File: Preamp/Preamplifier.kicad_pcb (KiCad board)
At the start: 2 copper layers, 100 x 100 mm, 155 parts, among them J1 Conn_01x03_Male, J12 XLR3, J14 Conn_01x03, J15 Conn_01x02, J16 Conn_01x02, J17 Conn_01x02, J2 Conn_01x02_Male, J3 Conn_01x02_Male, J4 Conn_01x03_Male, J5 Conn_01x03_Male, J6 Conn_01x02_Male, J7 Conn_01x03, J8 Conn_01x05_Female, Q1 2N3904, Q2 2N3906, Q3 2N3904, Q4 2N3906, Q5 BC549, SW1 SW_DPST, SW2 SW_SPDT, SW3 GND LIFT, SW4 SW_SPST, SW5 SW_HPFQ, U1 OPA2134, U2 NE5532, U3 NE5532, U4 NE5532, U5 TL072, U6 NE5532, U7 NE5532, U8 NE5532, U9 NE5532

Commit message: More layout work
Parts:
- removed C17: 100uF 50V, Capacitor_THT:CP_Radial_D8.0mm_P3.50mm
- removed C20, C21: 0.1uF, Capacitor_SMD:C_0805_2012Metric_Pad1.15x1.40mm_HandSolder
- removed D3, D4: 1N4148, Diode_THT:D_DO-35_SOD27_P7.62mm_Horizontal
- removed Q1: 2N3904, Package_TO_SOT_THT:TO-92_Inline
- removed Q2: 2N3906, Package_TO_SOT_THT:TO-92_Inline
- removed R15: 22k, Resistor_SMD:R_0805_2012Metric_Pad1.15x1.40mm_HandSolder
- removed R18, R23: 10K, Resistor_SMD:R_0805_2012Metric_Pad1.15x1.40mm_HandSolder
- removed R25, R26: 3.9k, Resistor_SMD:R_0805_2012Metric_Pad1.15x1.40mm_HandSolder
- removed R31: 10k, Resistor_SMD:R_0805_2012Metric_Pad1.15x1.40mm_HandSolder
- removed U3: NE5532, Package_DIP:DIP-8_W7.62mm_Socket
- C12, C15, C24, R10, R12, R20, R21, R42, R9: moved to B.Cu
- R11: value 10k -> 12k
- RV1: footprint Connector_PinHeader_2.54mm:PinHeader_2x03_P2.54mm_Vertical -> Connector_PinHeader_2.54mm:PinHeader_1x06_P2.54mm_Vertical
- RV2: value 1K log (headphone vol) -> 10k log (headphone vol); footprint Connector_PinHeader_2.54mm:PinHeader_2x03_P2.54mm_Vertical -> Connector_PinHeader_2.54mm:PinHeader_1x03_P2.54mm_Vertical
- SW1: value SW_DPST -> SW_HPF
- moved SW5 337.8 mm to (45.7, 94.9), turned to 270 degrees
- moved SW1 335.2 mm to (38.1, 94.9), turned to 270 degrees
- moved C1 281.9 mm to (130.8, 76.4), turned to 270 degrees
- moved C2 281.3 mm to (122.7, 76.4), turned to 270 degrees
- moved R9 268.9 mm to (128.3, 77.3), turned to 90 degrees
- moved C3 155.9 mm to (27.7, 86.1)
- moved R12 151.3 mm to (40.6, 96.5), turned to 90 degrees
- moved C6 148.7 mm to (31.9, 91.1)
- moved R13 145.2 mm to (32.0, 83.6), turned to 180 degrees
- moved C16 134.3 mm to (38.0, 89.3), turned to 90 degrees
- moved U2 131.0 mm to (35.7, 82.9), turned to 0 degrees
- moved C15 123.0 mm to (40.8, 83.9), turned to 90 degrees
- moved C9 121.6 mm to (46.6, 90.1), turned to 0 degrees
- moved R65 119.4 mm to (49.0, 91.1), turned to 270 degrees
- moved R17 115.1 mm to (49.0, 87.9), turned to 0 degrees
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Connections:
- R11 pad 1: EFXreturn -> GNDD
- R11 pad 2: Net-(R10-Pad2) -> GND
- R33 pad 1: Net-(R33-Pad1) -> Net-(J5-Pad3)
- R33 pad 2: Net-(C17-Pad2) -> Net-(R33-Pad2)
- R34 pad 1: Net-(R34-Pad1) -> Net-(J5-Pad2)
- R34 pad 2: Net-(C14-Pad2) -> Net-(R33-Pad2)
- R8 pad 2: Net-(R15-Pad1) -> Net-(R10-Pad2)
- R9 pad 2: Net-(R15-Pad1) -> Net-(R10-Pad2)
- RV2 pad 1: Net-(R33-Pad1) -> Net-(C14-Pad2)
- RV2 pad 2: Net-(J5-Pad3) -> Net-(R33-Pad2)
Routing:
- net Net-(C33-Pad2): track 37.5 -> 0.00 mm
- net -12V: track 132.5 -> 102.0 mm, vias 4 -> 1
- net Net-(C7-Pad2): track 17.4 -> 41.6 mm, vias 0 -> 1
- net Net-(C3-Pad1): track 0.00 -> 22.3 mm, vias 0 -> 1
- net Net-(C6-Pad1): track 0.00 -> 18.7 mm, vias 0 -> 1
- net +12V: track 129.5 -> 112.5 mm, vias 2 -> 3
- net FromEQ: track 0.00 -> 15.7 mm, vias 0 -> 1
- net LF: track 45.1 -> 30.3 mm
- net GND: track 7.90 -> 22.5 mm
- net GNDD: track 8.48 -> 19.0 mm
- net Net-(C7-Pad1): track 5.77 -> 15.0 mm
- net HF: track 18.6 -> 9.42 mm
- net Net-(C9-Pad1): track 5.89 -> 14.6 mm
- net Net-(C1-Pad2): track 0.00 -> 7.00 mm
- net Net-(C42-Pad2): track 6.00 -> 0.00 mm
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
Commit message: More layout
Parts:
- added H1: MountingHole, MountingHole:MountingHole_3.2mm_M3_ISO7380, F.Cu at (4.00, 96.0)
- added H2: MountingHole, MountingHole:MountingHole_3.2mm_M3_ISO7380, F.Cu at (103.3, 1.08)
- added H3: MountingHole, MountingHole:MountingHole_3.2mm_M3_ISO7380, F.Cu at (110.5, -6.17)
- added H4: MountingHole, MountingHole:MountingHole_3.2mm_M3_ISO7380, F.Cu at (110.5, 1.08)
- added J9: Conn_01x03, Connector_PinHeader_2.54mm:PinHeader_1x03_P2.54mm_Vertical, F.Cu at (5.08, 59.4)
- C36, C37, R29, R37, R38, R41, R44, R63: moved to B.Cu
- moved R37 365.7 mm to (35.6, 52.6), turned to 270 degrees
- moved D11 282.7 mm to (48.5, 115.7)
- moved SW3 121.4 mm to (58.4, 51.7), turned to 0 degrees
- moved J12 120.7 mm to (48.3, 51.7)
- moved R38 113.1 mm to (30.6, 52.2), turned to 270 degrees
- moved R41 108.5 mm to (26.6, 62.7), turned to 180 degrees
- moved R40 107.1 mm to (23.0, 55.6), turned to 270 degrees
- moved U6 106.6 mm to (27.8, 60.5), turned to 270 degrees
- moved C41 105.3 mm to (42.7, 73.8)
- moved C42 105.3 mm to (33.7, 73.8)
- moved C43 105.3 mm to (42.7, 61.2)
- moved C44 105.3 mm to (33.7, 61.2)
- moved C36 101.1 mm to (28.8, 66.1)
- moved R45 100.6 mm to (24.8, 71.1), turned to 180 degrees
- moved C37 100.4 mm to (20.1, 63.4), turned to 270 degrees
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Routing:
- net PreEQ: track 30.5 -> 66.7 mm, vias 1 -> 2
- net -12V: track 102.0 -> 132.5 mm
- net EFXreturn: track 16.0 -> 43.0 mm, vias 1 -> 3
- net Net-(D16-Pad2): track 9.51 -> 31.4 mm, vias 0 -> 1
- net LF: track 30.3 -> 8.67 mm, vias 1 -> 0
- net Net-(C44-Pad1): track 2.78 -> 23.6 mm
- net +12V: track 112.5 -> 133.2 mm
- net Tweeter: track 4.67 -> 19.0 mm
- net Net-(R38-Pad2): track 2.81 -> 16.5 mm
- net Net-(C43-Pad1): track 6.71 -> 17.0 mm
- net Net-(D11-Pad2): track 18.4 -> 28.2 mm, vias 0 -> 2
- net GND: track 22.5 -> 32.1 mm, vias 11 -> 9
- net Net-(C33-Pad2): track 0.00 -> 7.94 mm
- net GNDD: track 19.0 -> 11.4 mm
- net Net-(RV3-Pad1): track 0.00 -> 6.13 mm
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
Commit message: More layout work
Still need to lay out the headphone amplifier.
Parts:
- removed J7: Conn_01x03, TerminalBlock_Phoenix:TerminalBlock_Phoenix_MKDS-1,5-3_1x03_P5.00mm_Horizontal
- C22, R11, R30, R35, R36, R39, R43, R61, R64: moved to B.Cu
- D2: footprint Diode_THT:D_DO-35_SOD27_P7.62mm_Horizontal -> Diode_SMD:D_SOD-123; moved to B.Cu
- R48: moved to F.Cu
- moved R61 377.3 mm to (33.2, 96.6), turned to 270 degrees
- moved R30 369.8 mm to (39.5, 63.1), turned to 270 degrees
- moved R64 366.3 mm to (41.1, 89.2), turned to 270 degrees
- moved R39 361.0 mm to (56.6, 82.7), turned to 180 degrees
- moved R36 360.2 mm to (58.3, 87.0), turned to 180 degrees
- moved C22 355.6 mm to (66.3, 89.4), turned to 270 degrees
- moved C11 330.4 mm to (50.5, 80.0), turned to 90 degrees
- moved R35 328.3 mm to (62.4, 87.0), turned to 180 degrees
- moved R43 322.8 mm to (61.6, 98.8), turned to 180 degrees
- moved Q4 209.0 mm to (213.8, 74.4)
- moved C14 209.0 mm to (156.5, 96.6)
- moved Q3 209.0 mm to (188.8, 98.8)
- moved R27 209.0 mm to (197.3, 105.2)
- moved R28 209.0 mm to (185.4, 116.8)
- moved R32 209.0 mm to (209.3, 92.3)
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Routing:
- net +12V: track 133.2 -> 205.4 mm
- net -12V: track 132.5 -> 177.3 mm, vias 1 -> 3
- net LF: track 8.67 -> 52.7 mm
- net Net-(C5-Pad2): track 9.07 -> 43.7 mm, vias 0 -> 2
- net Overload: track 0.00 -> 33.1 mm
- net GNDD: track 11.4 -> 38.1 mm, vias 0 -> 2
- net Net-(C11-Pad2): track 0.00 -> 19.3 mm
- net Net-(D11-Pad2): track 28.2 -> 47.0 mm
- net Net-(R64-Pad2): track 0.00 -> 13.7 mm, vias 0 -> 3
- net HF: track 9.42 -> 23.1 mm
- net Net-(C11-Pad1): track 7.23 -> 19.4 mm
- net EFXsend: track 5.08 -> 13.0 mm, vias 0 -> 1
- net Net-(R35-Pad2): track 0.00 -> 4.60 mm
- net GND: track 32.1 -> 36.3 mm, vias 9 -> 11
- net Net-(C22-Pad2): track 4.80 -> 8.21 mm
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
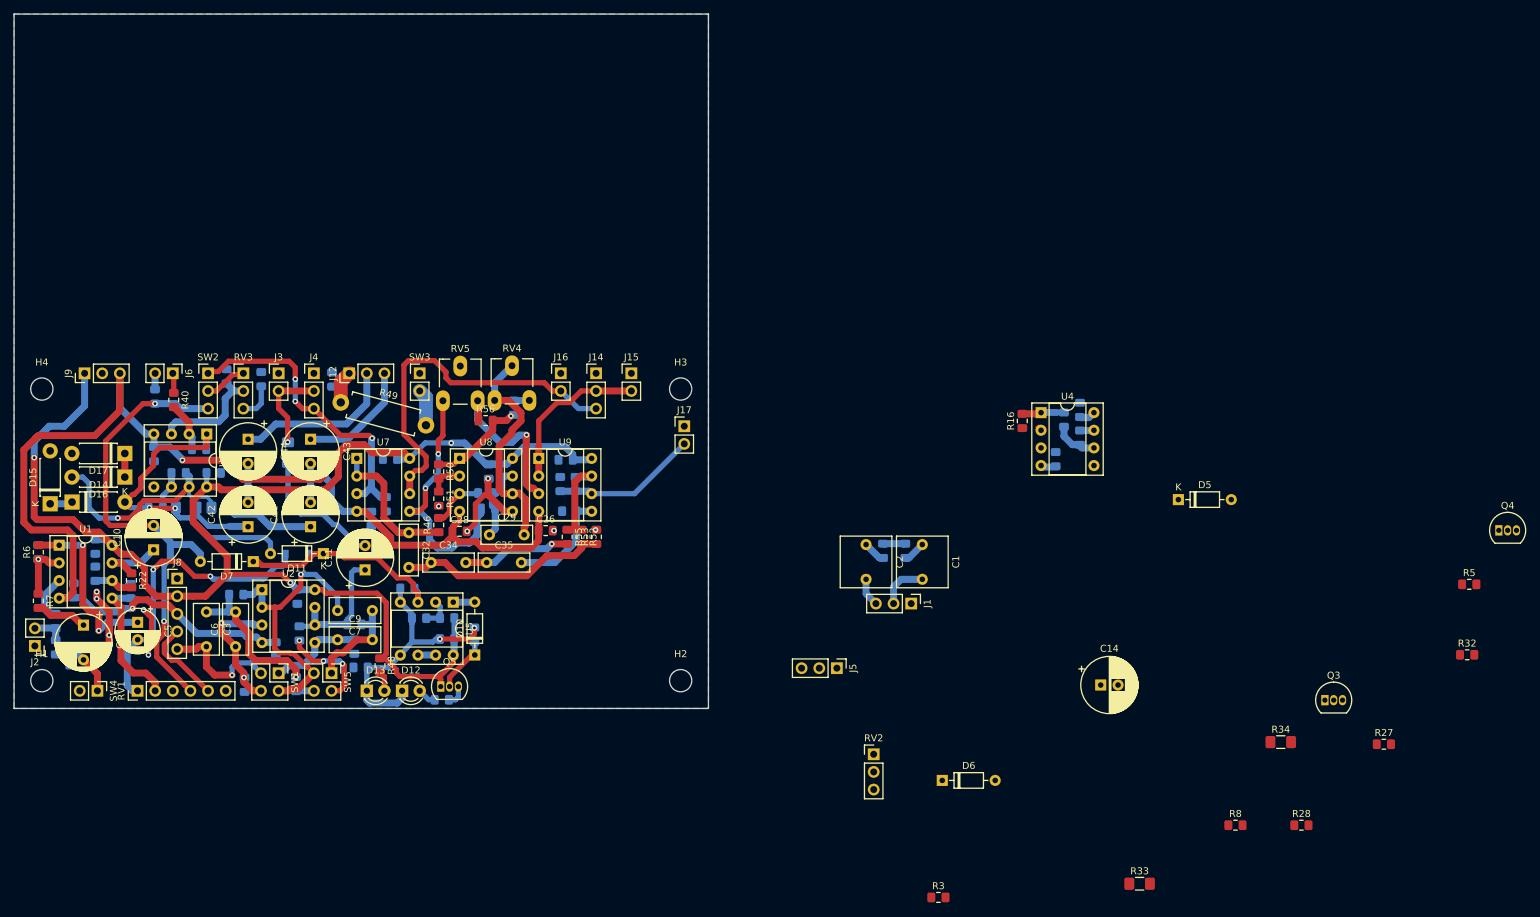
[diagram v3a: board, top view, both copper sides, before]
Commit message: Finished first pass at layout.
Still need to clean up silkscreen.
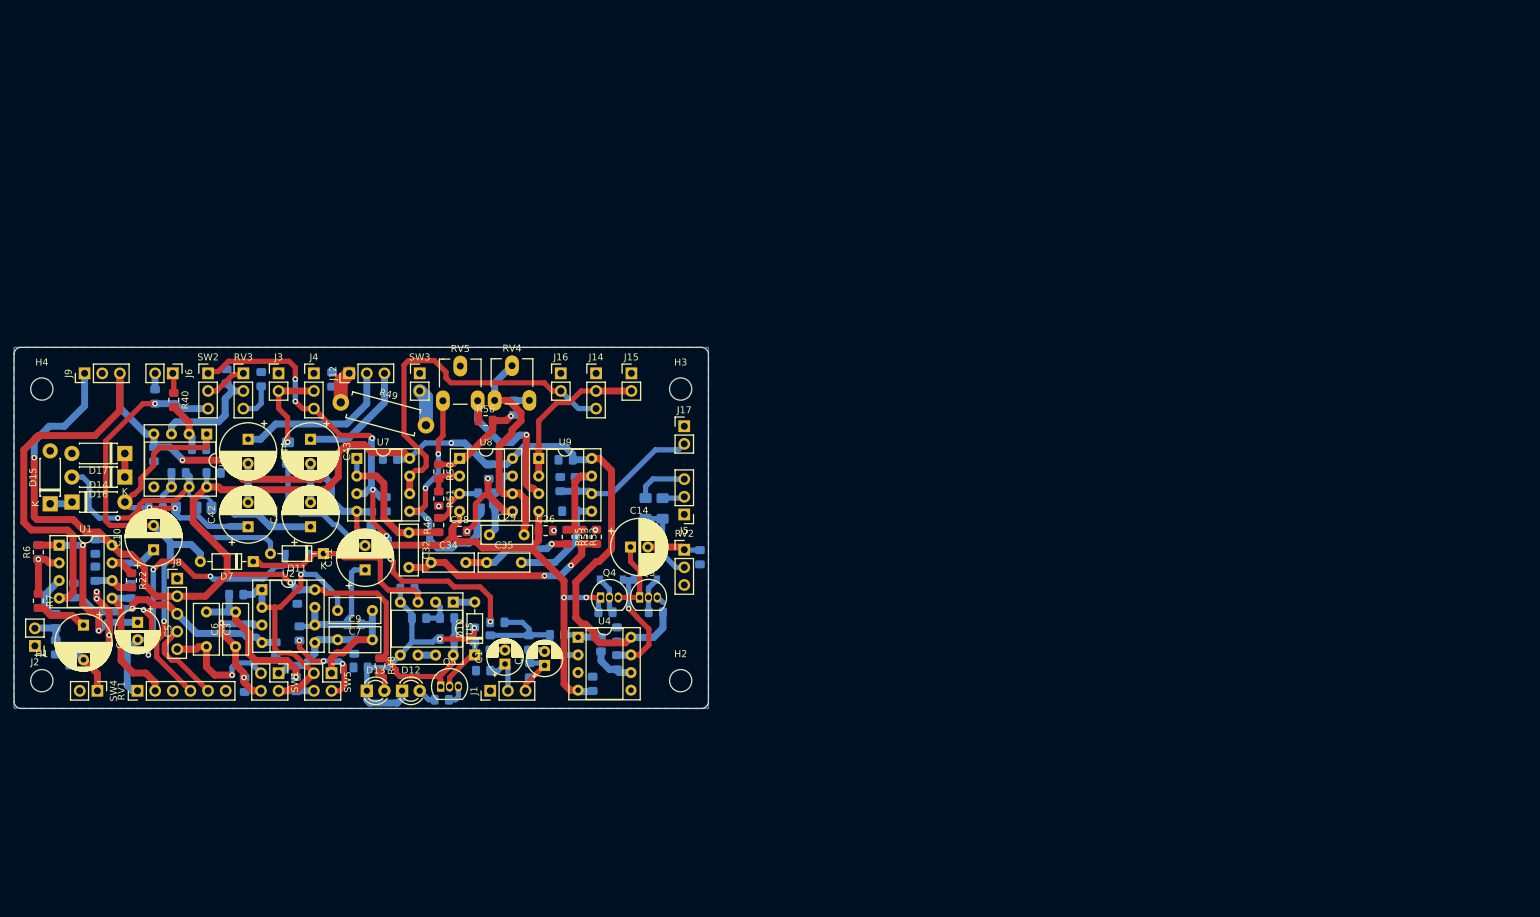
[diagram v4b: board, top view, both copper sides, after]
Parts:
- C1, C2: value 1uF -> 10uF 35V; footprint Capacitor_THT:C_Rect_L7.2mm_W7.2mm_P5.00mm_FKS2_FKP2_MKS2_MKP2 -> Capacitor_THT:CP_Radial_D5.0mm_P2.00mm
- D5, D6: footprint Diode_THT:D_DO-35_SOD27_P7.62mm_Horizontal -> Diode_SMD:D_SOD-123; moved to B.Cu
- R16, R27, R28, R3, R32, R33, R34, R5, R8: moved to B.Cu
- moved R5 142.6 mm to (67.5, 94.5), turned to 180 degrees
- moved Q4 129.7 mm to (84.5, 84.0)
- moved R32 111.4 mm to (98.8, 78.2), turned to 270 degrees
- moved R8 110.2 mm to (69.6, 87.6)
- moved R27 106.6 mm to (92.4, 86.2), turned to 180 degrees
- moved R28 104.8 mm to (85.2, 86.2), turned to 180 degrees
- moved Q3 99.8 mm to (90.1, 84.0)
- moved R34 95.2 mm to (93.4, 71.2), turned to 270 degrees
- moved R33 89.4 mm to (91.0, 71.2), turned to 270 degrees
- moved D5 77.6 mm to (90.9, 81.5)
- moved C19 74.1 mm to (83.3, 96.5)
- moved U4 74.1 mm to (81.2, 89.8)
- moved C18 74.1 mm to (86.8, 89.3)
- moved R19 74.1 mm to (84.5, 90.8)
- moved R24 74.1 mm to (86.8, 93.3)
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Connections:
- J1 pad 2: Net-(C1-Pad2) -> Net-(C1-Pad1)
- J1 pad 3: Net-(C2-Pad2) -> Net-(C2-Pad1)
- R10 pad 1: Net-(C2-Pad1) -> Net-(C2-Pad2)
- R3 pad 1: Net-(C2-Pad2) -> Net-(C2-Pad1)
- R5 pad 1: Net-(C1-Pad2) -> Net-(C1-Pad1)
- R9 pad 1: Net-(C1-Pad1) -> Net-(C1-Pad2)
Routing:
- net +12V: track 205.4 -> 251.3 mm
- net -12V: track 177.3 -> 210.4 mm, vias 3 -> 5
- net EFXreturn: track 44.1 -> 76.3 mm, vias 3 -> 7
- net Net-(R10-Pad2): track 3.65 -> 19.4 mm
- net Net-(D5-Pad1): track 2.03 -> 17.4 mm, vias 0 -> 1
- net Net-(R33-Pad2): track 0.00 -> 11.4 mm
- net Net-(C14-Pad1): track 0.00 -> 10.9 mm
- net Net-(J5-Pad3): track 0.00 -> 7.72 mm
- net Net-(C14-Pad2): track 0.00 -> 7.69 mm
- net Net-(D6-Pad1): track 0.00 -> 5.46 mm
- net Net-(D5-Pad2): track 0.00 -> 5.22 mm
- net Net-(C1-Pad2): track 7.00 -> 2.13 mm
- net Net-(C2-Pad1): track 3.25 -> 7.08 mm
- net Net-(C1-Pad1): track 3.25 -> 6.55 mm
- net Net-(J5-Pad2): track 0.00 -> 3.20 mm
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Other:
- board size 100 x 100 mm -> 100 x 52 mm

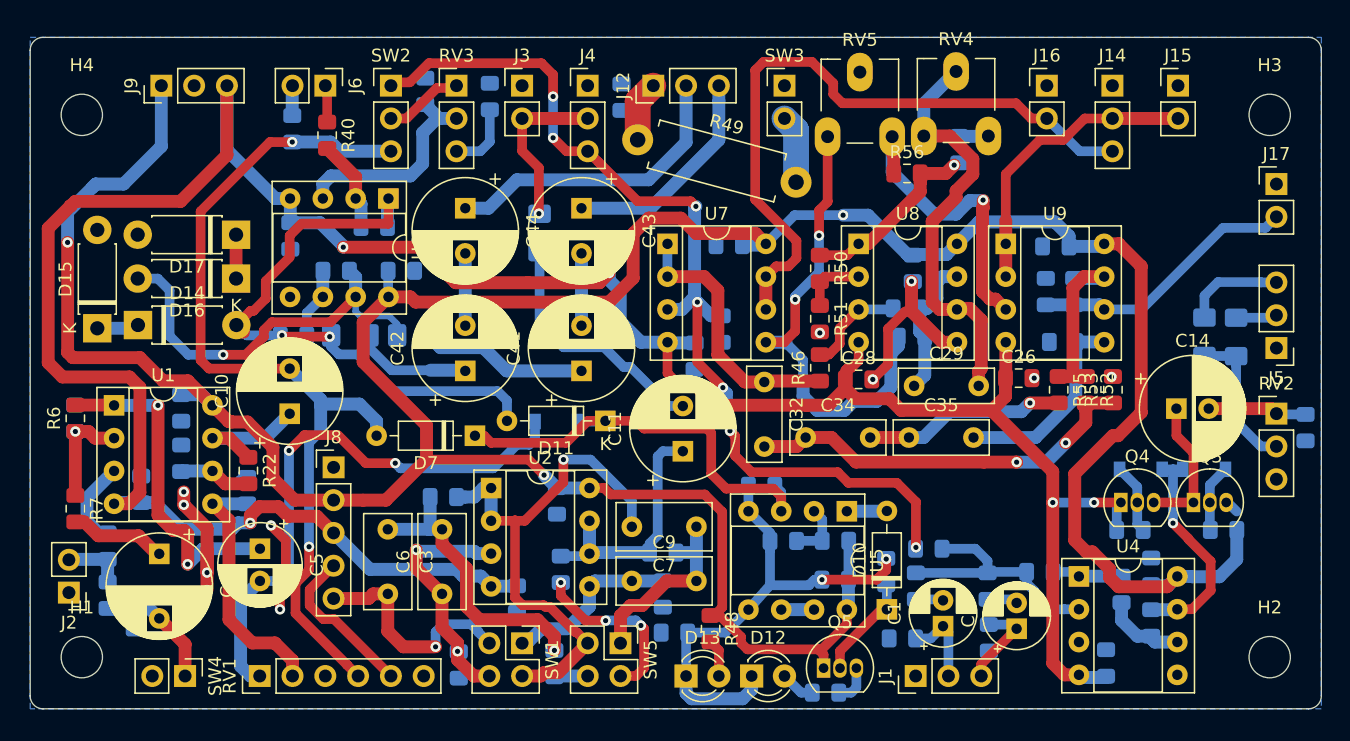
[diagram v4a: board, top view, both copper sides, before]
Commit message: Cleaned up silk screen + made Gerbers
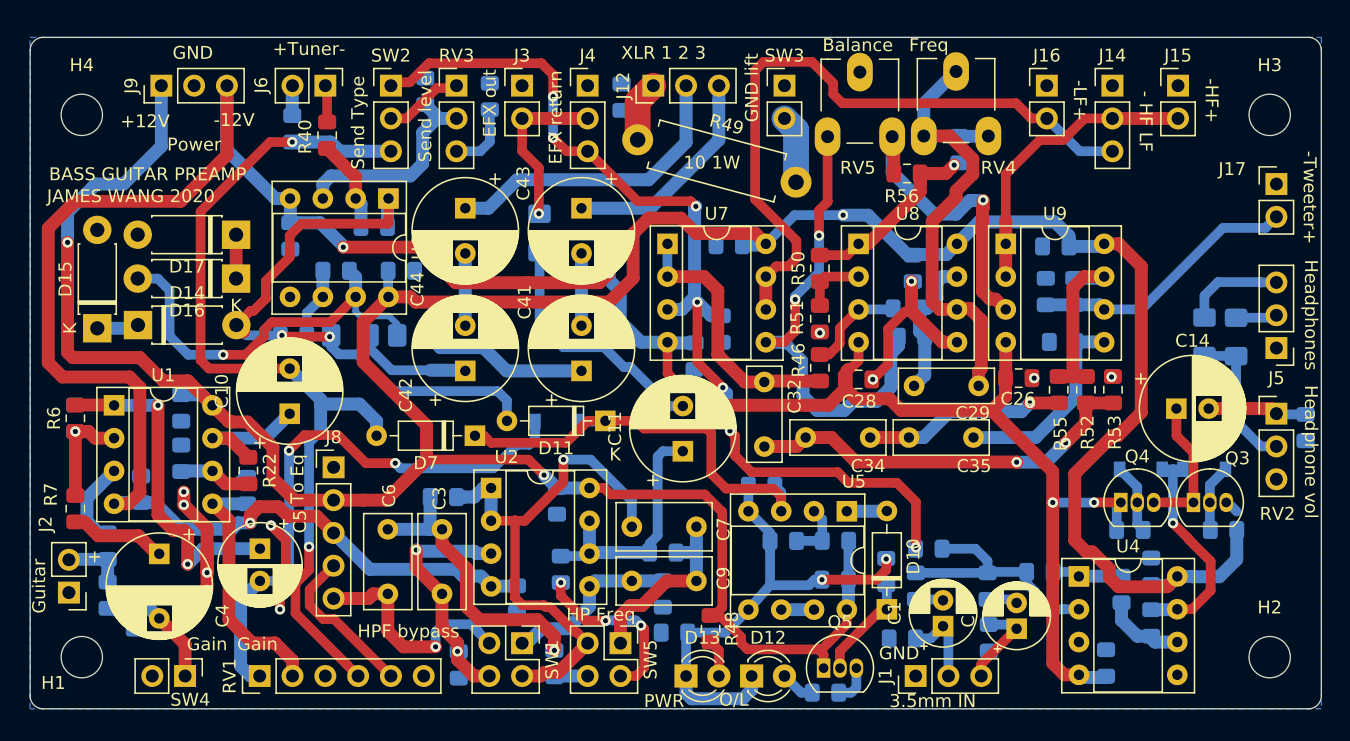
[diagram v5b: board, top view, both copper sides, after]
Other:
- board text added: "+"
- board text added: "+12V"
- board text added: "+Tuner-"
- board text added: "- HF LF"
- board text added: "-12V"
- board text added: "-HF+"
- board text added: "-LF+"
- board text added: "-Tweeter+"
- board text added: "1 2 3"
- board text added: "10 1W"
- board text added: "3.5mm IN"
- board text added: "BASS GUITAR PREAMP"
- board text added: "Balance"
- board text added: "EFX out"
- board text added: "EFX return"
- board text added: "Freq"
- board text added: "GND"
- board text added: "GND lift"
- board text added: "Gain"
- board text added: "Guitar"
- board text added: "HP Freq"
- board text added: "HPF bypass"
- board text added: "Headphone vol"
- board text added: "Headphones"
- board text added: "JAMES WANG 2020"
- board text added: "O/L"
- board text added: "PWR"
- board text added: "Power"
- board text added: "Send Type"
- board text added: "Send level"
- board text added: "To Eq"
- board text added: "XLR"
